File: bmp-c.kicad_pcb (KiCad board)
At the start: 4 copper layers, 35 x 15 mm, 60 parts, among them J1 USB_C_Receptacle_USB2.0, J2 Conn_01x10, J3 Conn_01x04, J4 JTAG-10, Q1 DMG1023DV, Q2 DMG1024UV, SW1 SW_SPST, U1 USBLC6-2P6, U2 SN74LVC2T45YZPR, U3 SN74LVC2T45YZPR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

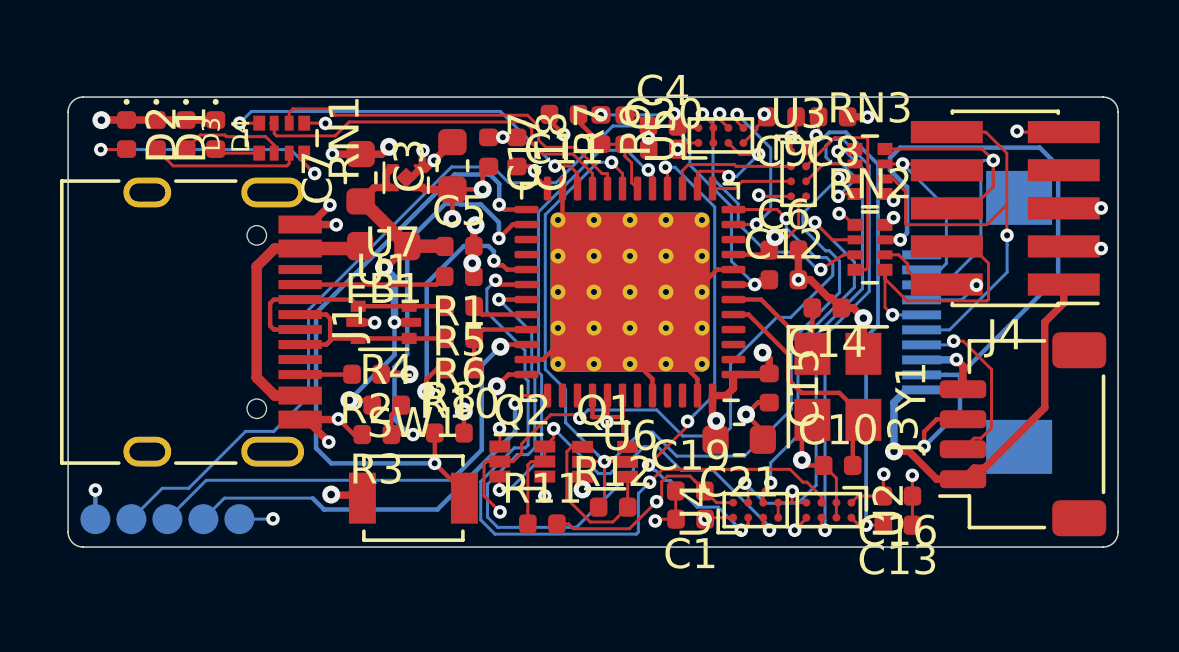
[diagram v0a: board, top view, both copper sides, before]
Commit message: Silkscreen improvementrs
Signed-off-by: Dominik Sliwa <dominik@e-plum.pl>
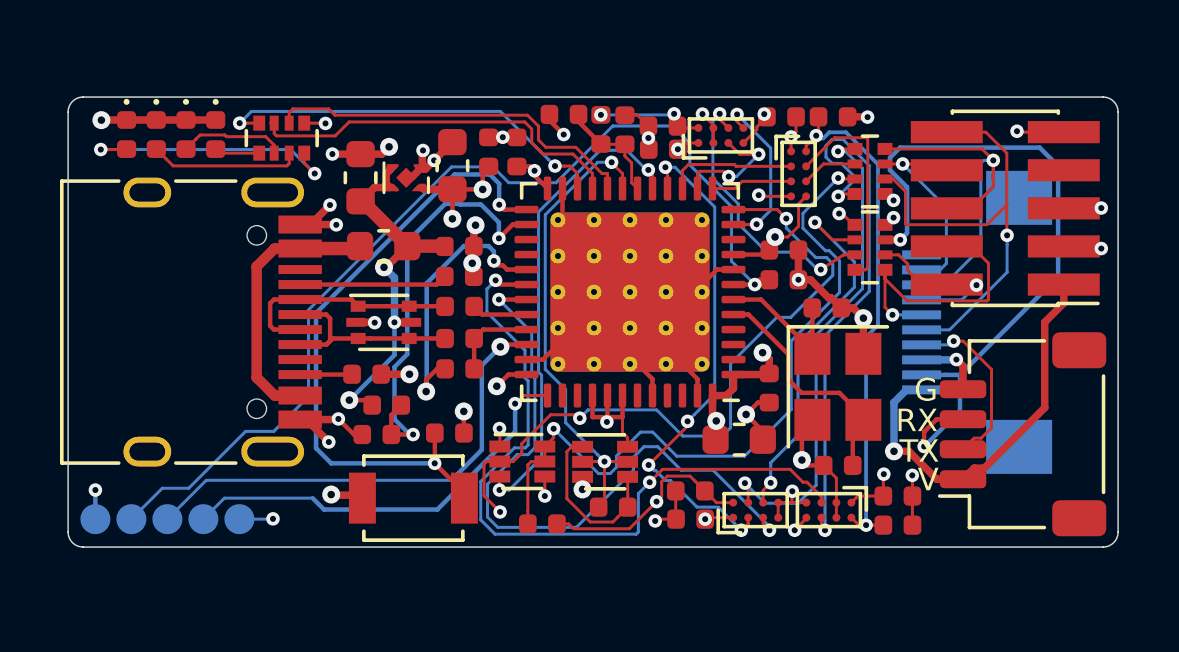
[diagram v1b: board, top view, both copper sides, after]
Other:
- board text added: "(c) 2019 CC-BY-SA @randomplum dominik@sliwa.io"
- board text added: "G"
- board text added: "RX"
- board text added: "TX"
- board text added: "V"

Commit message: use kicad library symbol for ncp114
Signed-off-by: Dominik Sliwa <dominik@e-plum.pl>
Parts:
- U7: value NCP114MX -> NCP114xMXxxxTxG
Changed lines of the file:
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@@
   )
   (layers
-    (0 F.Cu signal hide)
+    (0 F.Cu signal)
     (1 In1.Cu signal hide)
     (2 In2.Cu signal hide)
-    (31 B.Cu signal)
+    (31 B.Cu signal hide)
     (32 B.Adhes user hide)
     (33 F.Adhes user hide)
@@
       (effects (font (size 1 1) (thickness 0.15)))
     )
-    (fp_text value NCP114MX (at 0.47 2.34) (layer F.Fab)
-      (effects (font (size 1 1) (thickness 0.15)))
-    )
+    (fp_text value NCP114xMXxxxTxG (at 0.47 2.34) (layer F.Fab)
+      (effects (font (size 1 1) (thickness 0.15)))
+    )
